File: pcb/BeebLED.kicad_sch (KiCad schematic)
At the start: 13 parts, among them J1 BBC User Port, J2 Jack-DC, U1 74HC14, U2 74LS165, X1 8Mhz

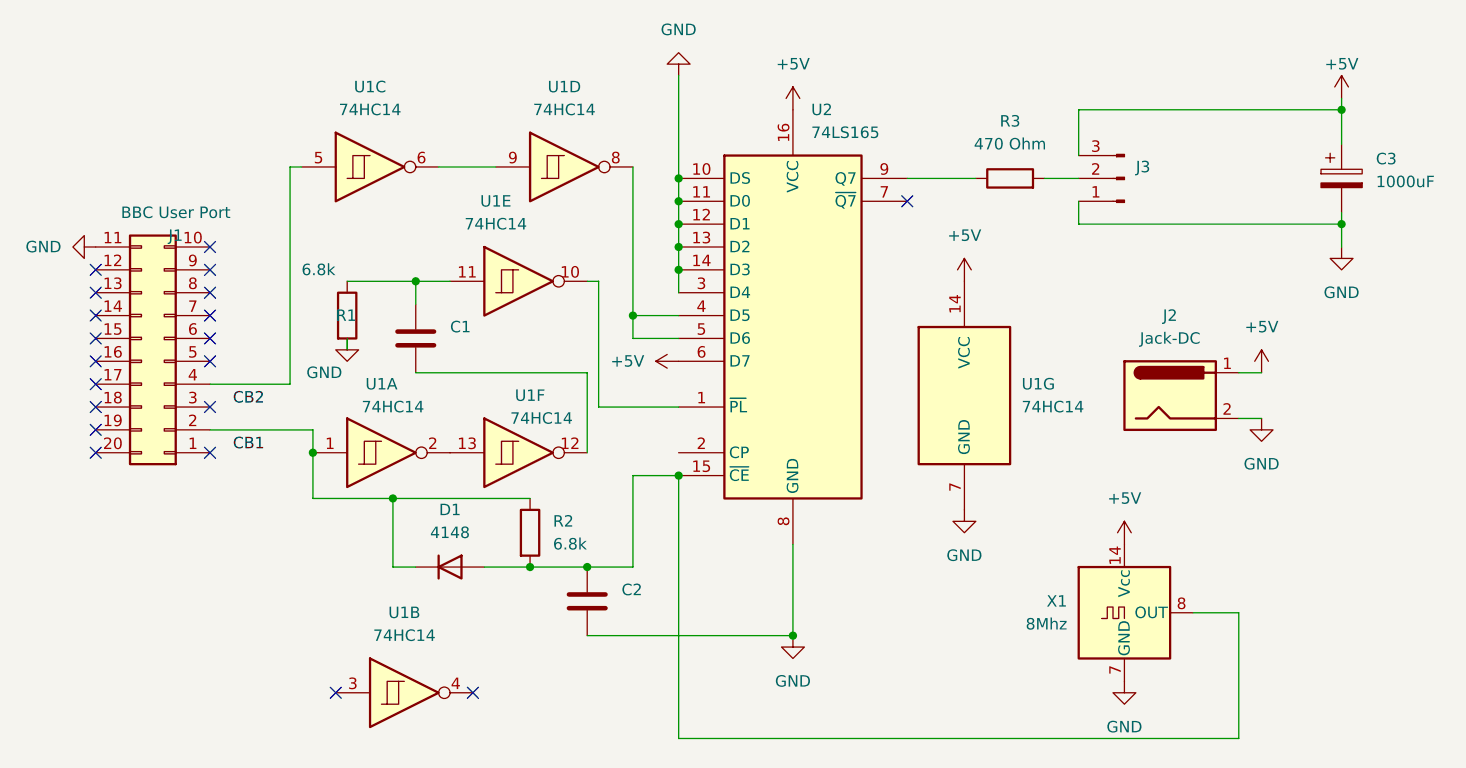
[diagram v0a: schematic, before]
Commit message: Fixed 8 Mhz not connected
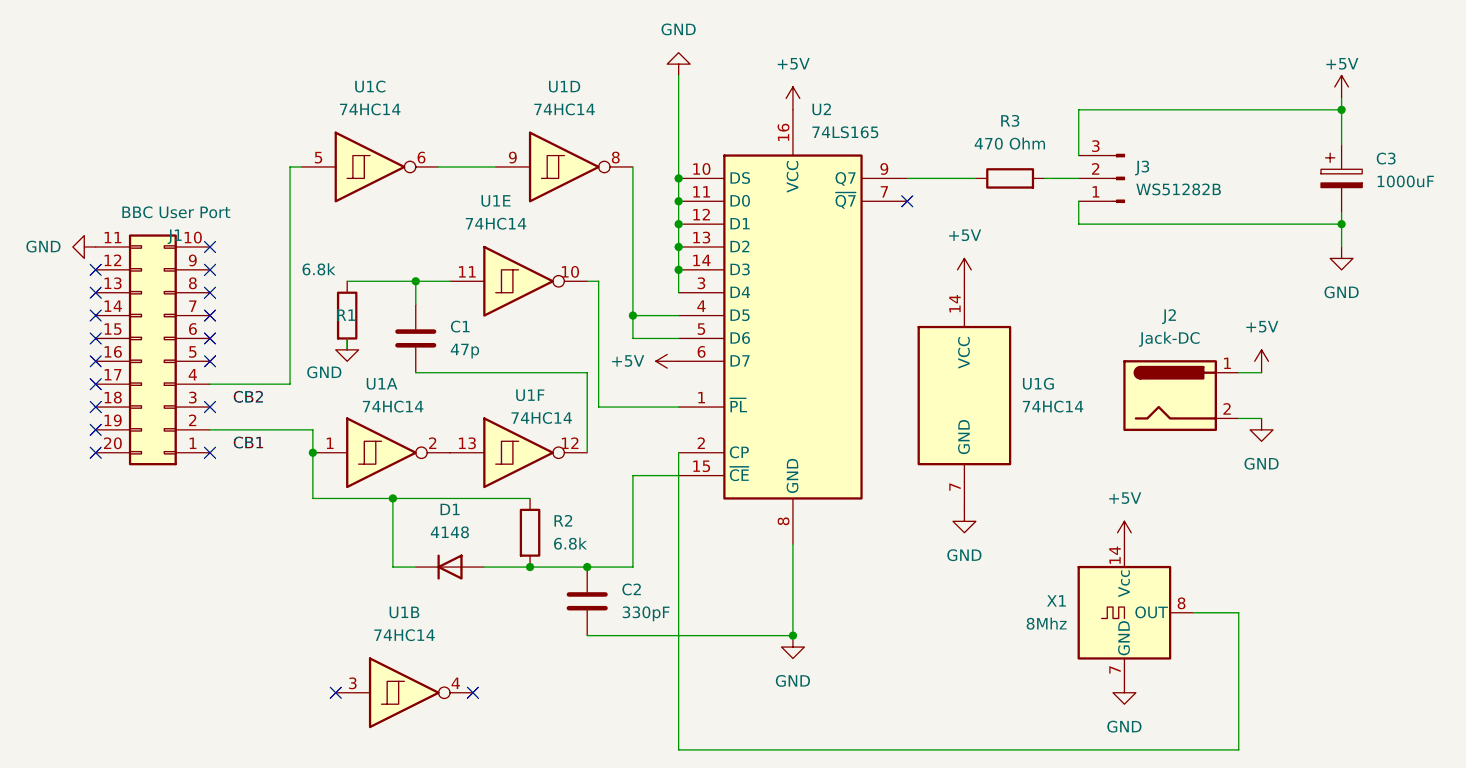
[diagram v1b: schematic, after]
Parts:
- C1: value (none) -> 47p; footprint (none) -> Capacitor_THT:C_Disc_D5.0mm_W2.5mm_P2.50mm
- C2: value (none) -> 330pF; footprint (none) -> Capacitor_THT:C_Disc_D5.0mm_W2.5mm_P2.50mm
- J3: value (none) -> WS51282B
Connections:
- net at C2.1, D1.1 (A), R2.2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: no longer X1.8 (OUT)
- net at U2.2 (CP): now also X1.8 (OUT)
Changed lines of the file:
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@@
   (junction (at 140.97 81.28) (diameter 0) (color 0 0 0 0)
-  )
-  (junction (at 140.97 109.22) (diameter 0) (color 0 0 0 0)
   )
   (junction (at 111.76 87.63) (diameter 0) (color 0 0 0 0)
@@
   (no_connect (at 166.37 78.74))
   (no_connect (at 118.11 133.35))
-  (wire (pts (xy 140.97 109.22) (xy 140.97 138.43))
-    (stroke (width 0) (type default) (color 0 0 0 0))
-  )
   (wire (pts (xy 214.63 81.28) (xy 214.63 80.01))
     (stroke (width 0) (type default) (color 0 0 0 0))
@@
     (stroke (width 0) (type default) (color 0 0 0 0))
   )
-  (wire (pts (xy 203.2 138.43) (xy 203.2 124.46))
-    (stroke (width 0) (type default) (color 0 0 0 0))
-  )
   (wire (pts (xy 140.97 86.36) (xy 140.97 88.9))
     (stroke (width 0) (type default) (color 0 0 0 0))
@@
     (stroke (width 0) (type default) (color 0 0 0 0))
   )
+  (wire (pts (xy 203.2 124.46) (xy 203.2 139.7))
+    (stroke (width 0) (type default) (color 0 0 0 0))
+  )
   (wire (pts (xy 140.97 64.77) (xy 140.97 76.2))
     (stroke (width 0) (type default) (color 0 0 0 0))
@@
     (stroke (width 0) (type default) (color 0 0 0 0))
   )
+  (wire (pts (xy 140.97 106.68) (xy 140.97 139.7))
+    (stroke (width 0) (type default) (color 0 0 0 0))
+  )
   (wire (pts (xy 198.12 124.46) (xy 203.2 124.46))
     (stroke (width 0) (type default) (color 0 0 0 0))
@@
     (stroke (width 0) (type default) (color 0 0 0 0))
   )
-  (wire (pts (xy 140.97 138.43) (xy 203.2 138.43))
-    (stroke (width 0) (type default) (color 0 0 0 0))
-  )
   (wire (pts (xy 135.89 74.93) (xy 135.89 91.44))
     (stroke (width 0) (type default) (color 0 0 0 0))
   )
   (wire (pts (xy 130.81 97.79) (xy 111.76 97.79))
+    (stroke (width 0) (type default) (color 0 0 0 0))
+  )
+  (wire (pts (xy 140.97 139.7) (xy 203.2 139.7))
     (stroke (width 0) (type default) (color 0 0 0 0))
   )
@@
       (effects (font (size 1.27 1.27)) (justify left))
     )
-    (property "Value" "" (id 1) (at 115.57 95.2499 0)
-      (effects (font (size 1.27 1.27)) (justify left))
-    )
-    (property "Footprint" "" (id 2) (at 112.7252 97.79 0)
+    (property "Value" "47p" (id 1) (at 115.57 95.2499 0)
+      (effects (font (size 1.27 1.27)) (justify left))
+    )
+    (property "Footprint" "Capacitor_THT:C_Disc_D5.0mm_W2.5mm_P2.50mm" (id 2) (at 112.7252 97.79 0)
       (effects (font (size 1.27 1.27)) hide)
     )
@@
       (effects (font (size 1.27 1.27)) (justify left))
     )
-    (property "Value" "" (id 1) (at 134.62 124.4599 0)
-      (effects (font (size 1.27 1.27)) (justify left))
-    )
-    (property "Footprint" "" (id 2) (at 131.7752 127 0)
+    (property "Value" "330pF" (id 1) (at 134.62 124.4599 0)
+      (effects (font (size 1.27 1.27)) (justify left))
+    )
+    (property "Footprint" "Capacitor_THT:C_Disc_D5.0mm_W2.5mm_P2.50mm" (id 2) (at 131.7752 127 0)
       (effects (font (size 1.27 1.27)) hide)
     )
@@
       (effects (font (size 1.27 1.27)) (justify right))
     )
-    (property "Value" "" (id 1) (at 191.77 77.4699 0)
+    (property "Value" "WS51282B" (id 1) (at 191.77 77.4699 0)
       (effects (font (size 1.27 1.27)) (justify right))
     )

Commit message: Changed J3 connector type and tied U1 Pin 3 to GND
Thanks to the advice from stardot! :-)
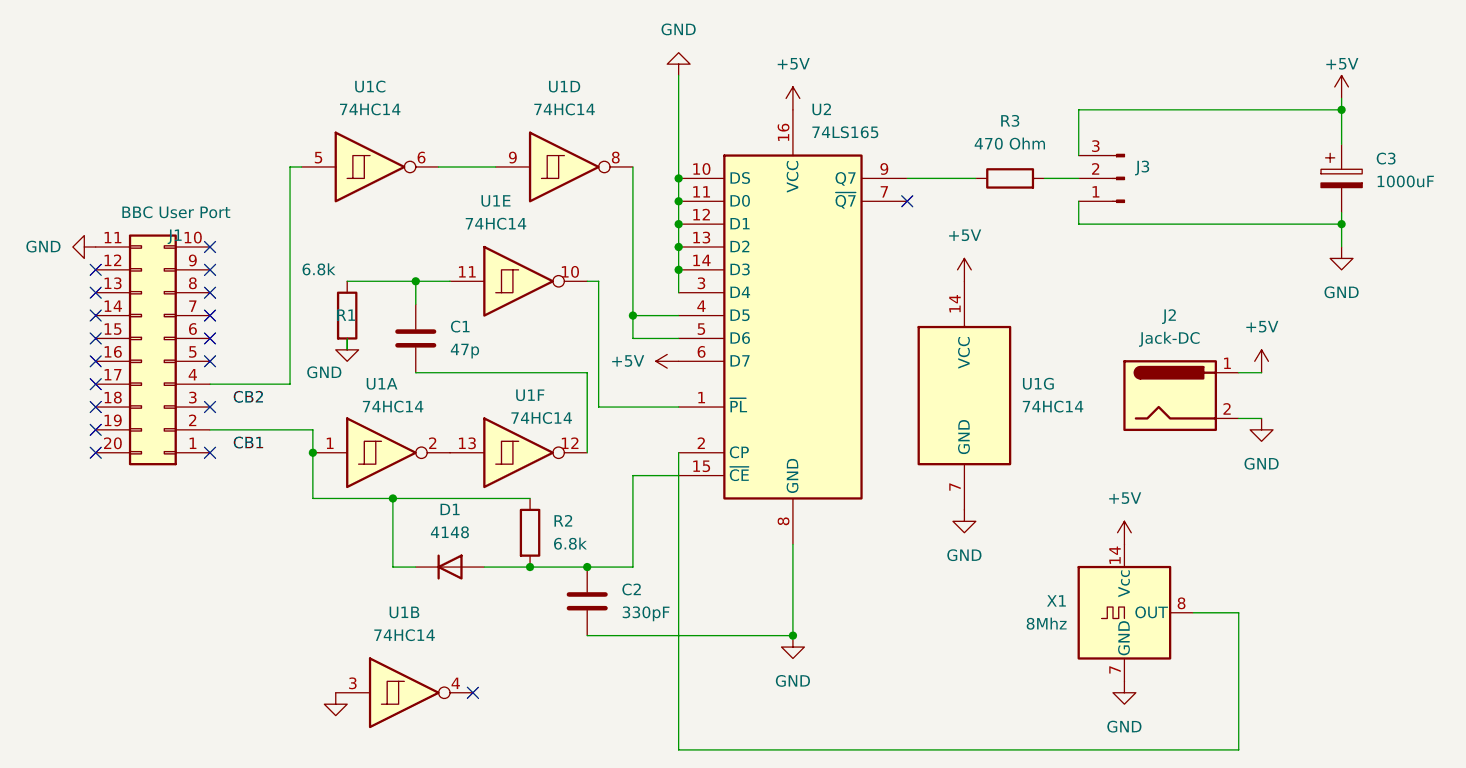
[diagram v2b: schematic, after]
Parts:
- J3: value WS51282B -> (none); footprint Connector_JST:JST_EH_S3B-EH_1x03_P2.50mm_Horizontal -> (none)
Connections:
- net GND: now also U1.3
- no-connect marks 20 -> 19
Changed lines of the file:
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@@
   (no_connect (at 76.2 93.98))
   (no_connect (at 76.2 96.52))
-  (no_connect (at 102.87 133.35))
   (no_connect (at 166.37 78.74))
   (no_connect (at 118.11 133.35))
@@
     )
     (property "Datasheet" "" (id 3) (at 172.72 87.63 0)
+      (effects (font (size 1.27 1.27)) hide)
+    )
+    (pin "1")
+  )
+  (symbol (lib_id "power:GND") (at 102.87 133.35 0) (unit 1)
+    (in_bom yes) (on_board yes) (fields_autoplaced)
+    (property "Reference" "#PWR?" (id 0) (at 102.87 139.7 0)
+      (effects (font (size 1.27 1.27)) hide)
+    )
+    (property "Value" "" (id 1) (at 102.87 138.43 0))
+    (property "Footprint" "" (id 2) (at 102.87 133.35 0)
+      (effects (font (size 1.27 1.27)) hide)
+    )
+    (property "Datasheet" "" (id 3) (at 102.87 133.35 0)
       (effects (font (size 1.27 1.27)) hide)
     )
@@
   )
   (symbol (lib_id "Connector:Conn_01x03_Male") (at 190.5 76.2 180) (unit 1)
-    (in_bom yes) (on_board yes) (fields_autoplaced)
+    (in_bom yes) (on_board yes)
     (property "Reference" "J3" (id 0) (at 191.77 74.9299 0)
       (effects (font (size 1.27 1.27)) (justify right))
     )
-    (property "Value" "WS51282B" (id 1) (at 191.77 77.4699 0)
+    (property "Value" "" (id 1) (at 191.77 77.4699 0)
       (effects (font (size 1.27 1.27)) (justify right))
     )
-    (property "Footprint" "Connector_JST:JST_EH_S3B-EH_1x03_P2.50mm_Horizontal" (id 2) (at 190.5 76.2 0)
+    (property "Footprint" "" (id 2) (at 190.5 76.2 0)
       (effects (font (size 1.27 1.27)) hide)
     )
@@
       (reference "#PWR0114") (unit 1) (value "+5V") (footprint "")
     )
+    (path "/22e8adfd-f463-4836-99f0-c98388c7ac27"
+      (reference "#PWR?") (unit 1) (value "GND") (footprint "")
+    )
     (path "/65ed6649-7f77-42ba-8364-96e8d5d3ec59"
       (reference "C1") (unit 1) (value "47p") (footprint "Capacitor_THT:C_Disc_D5.0mm_W2.5mm_P2.50mm")
@@
     )
     (path "/cbc4f504-99b1-404f-8b3a-f0881c4b1ae5"
-      (reference "J3") (unit 1) (value "WS51282B") (footprint "Connector_JST:JST_EH_S3B-EH_1x03_P2.50mm_Horizontal")
+      (reference "J3") (unit 1) (value "WS51282B") (footprint "Connector_JST:JST_PH_S3B-PH-K_1x03_P2.00mm_Horizontal")
     )
     (path "/f0c486ea-8fdb-49cc-877f-2ed6f80e037d"
